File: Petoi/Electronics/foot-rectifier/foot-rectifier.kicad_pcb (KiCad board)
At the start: 2 copper layers, 6 parts, among them J1 Conn_01x04_Male, J2 Conn_01x02_Male

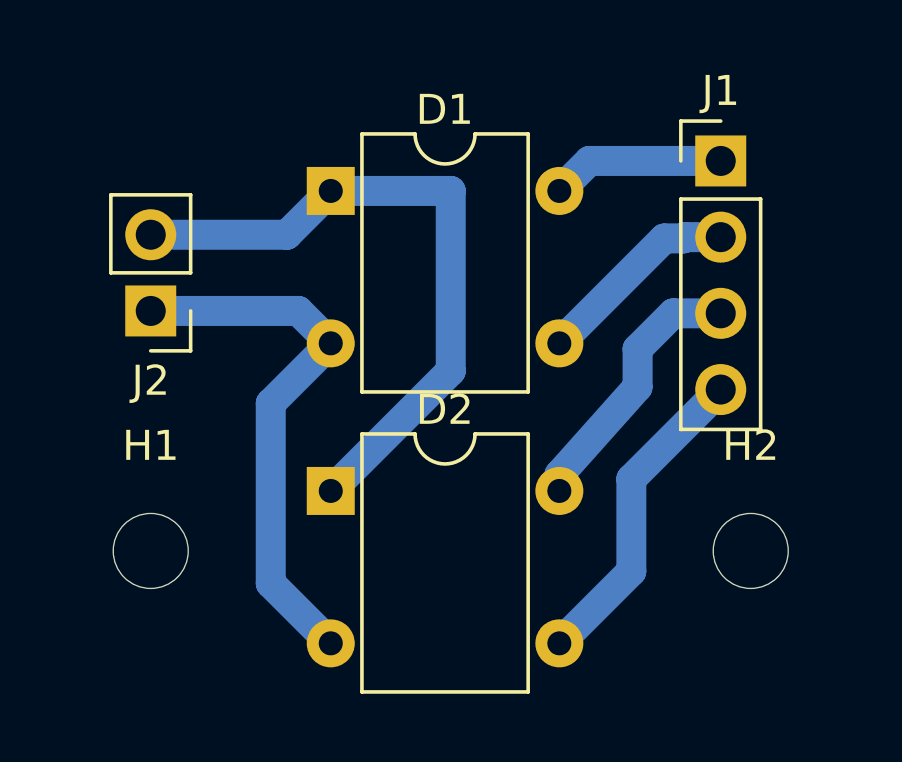
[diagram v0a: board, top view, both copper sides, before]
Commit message: Foot power circuit added. RRL-OpenCat created with everything in a flat single folder as a single Arduino project for ease of editing.
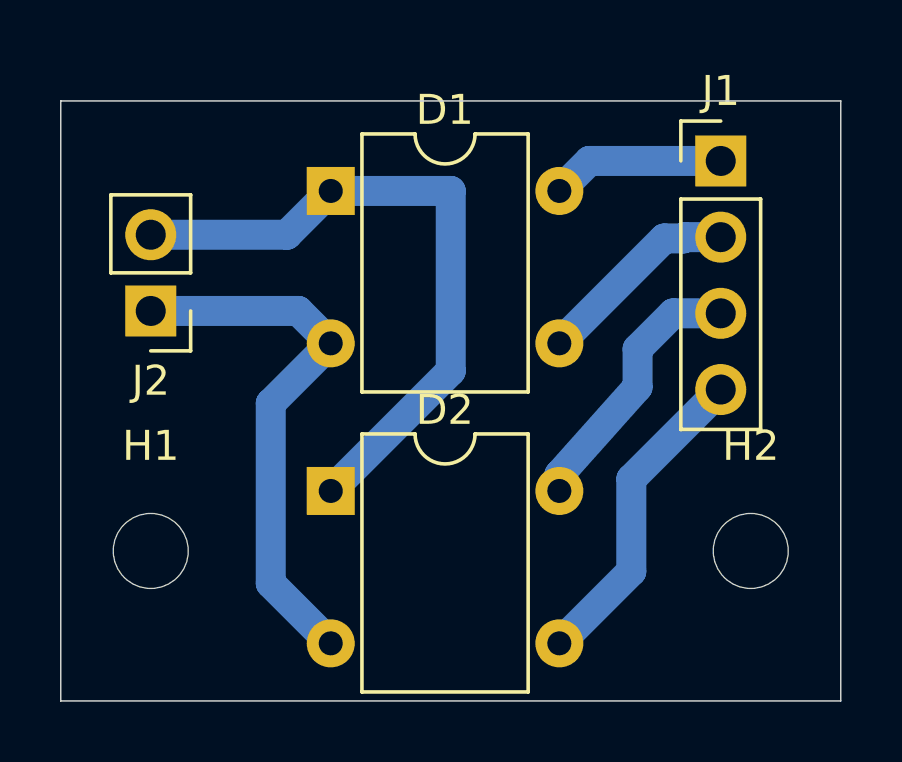
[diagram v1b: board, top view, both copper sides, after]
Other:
- board outline added: 26 x 20 mm
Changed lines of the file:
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@@
   (general
     (thickness 1.6)
-    (drawings 0)
+    (drawings 4)
     (tracks 24)
     (zones 0)
@@
   )
   (setup
-    (last_trace_width 1)
+    (last_trace_width 0.25)
     (user_trace_width 1)
     (trace_clearance 0.2)
@@
     (visible_elements FFFFFF7F)
     (pcbplotparams
-      (layerselection 0x010fc_ffffffff)
+      (layerselection 0x01000_fffffffe)
       (usegerberextensions false)
       (usegerberattributes false)
@@
       (outputformat 1)
       (mirror false)
-      (drillshape 1)
+      (drillshape 0)
       (scaleselection 1)
-      (outputdirectory ""))
+      (outputdirectory "GERBER/"))
   )
   (net 0 "")
@@
     (pad 1 np_thru_hole circle (at 0 0) (size 2.5 2.5) (drill 2.5) (layers *.Cu *.Mask))
   )
+  (gr_line (start 146 -11) (end 146 -31) (layer Edge.Cuts) (width 0.05))
+  (gr_line (start 172 -11) (end 146 -11) (layer Edge.Cuts) (width 0.05))
+  (gr_line (start 172 -31) (end 172 -11) (layer Edge.Cuts) (width 0.05))
+  (gr_line (start 146 -31) (end 172 -31) (layer Edge.Cuts) (width 0.05))
   (segment (start 163.62 -29) (end 162.62 -28) (width 1) (layer B.Cu) (net 1))
   (segment (start 168 -29) (end 163.62 -29) (width 1) (layer B.Cu) (net 1))

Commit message: Sally's updated designs.
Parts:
- added C1: 0.1u, Capacitor_SMD:C_0805_2012Metric, B.Cu at (95.9, -54.1)
- added C2: 0.1u, Capacitor_SMD:C_0805_2012Metric, B.Cu at (88.0, -51.3)
- added C3: 0.1u, Capacitor_SMD:C_0805_2012Metric, B.Cu at (95.9, -63.5)
- added H3: MountingHole, MountingHole:MountingHole_2.5mm, F.Cu at (102.5, -61.5)
- added H4: MountingHole, MountingHole:MountingHole_2.5mm, F.Cu at (102.5, -3.50)
- added J3: I2C, Connector_PinSocket_2.54mm:PinSocket_1x04_P2.54mm_Vertical, F.Cu at (96.9, -60.5)
- added J4: range, Connector_PinSocket_2.54mm:PinSocket_1x04_P2.54mm_Vertical, F.Cu at (96.9, -57.0)
- added U1: LTC2990, Package_SO:MSOP-10_3x3mm_P0.5mm, B.Cu at (84.5, -50.0)
- J1: value Conn_01x04_Male -> Legs; footprint Connector_PinHeader_2.54mm:PinHeader_1x04_P2.54mm_Vertical -> Connector_PinSocket_2.54mm:PinSocket_1x16_P2.54mm_Vertical
- J2: value Conn_01x02_Male -> USB pwr out
- moved H2 96.9 mm to (83.5, -61.5)
- moved J1 70.6 mm to (100.8, -50.6)
- moved D2 70.1 mm to (85.1, -13.0), turned to 90 degrees
- moved D1 69.9 mm to (85.2, -23.7), turned to 90 degrees
- moved H1 66.7 mm to (83.5, -3.50)
- moved J2 59.4 mm to (91.5, -8.90), turned to 90 degrees
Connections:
- J1 pad 2: Net-(D1-Pad3) -> GND
- J1 pad 3: Net-(D2-Pad4) -> +3V3
- J1 pad 4: Net-(D2-Pad3) -> Net-(J1-Pad4)
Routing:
- net +3V3: track 0.00 -> 84.8 mm
- net GND: track 0.00 -> 75.6 mm, vias 0 -> 6
- net Net-(J1-Pad16): track 0.00 -> 70.5 mm
- net Net-(J1-Pad12): track 0.00 -> 35.8 mm, vias 0 -> 2
- net Net-(J1-Pad8): track 0.00 -> 24.2 mm
- net SDA: track 0.00 -> 23.6 mm
- net Net-(D1-Pad4): track 5.79 -> 28.9 mm, vias 0 -> 2
- net Net-(J1-Pad4): track 0.00 -> 17.9 mm
- net SCL: track 0.00 -> 12.1 mm
- net Net-(D1-Pad3): track 6.85 -> 19.0 mm, vias 0 -> 2
- net Net-(D2-Pad4): track 8.99 -> 20.7 mm
- net Net-(D1-Pad1): track 22.3 -> 30.9 mm
- added copper zone on B.Cu, net GND
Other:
- board size 26 x 20 mm -> 26 x 65 mm
